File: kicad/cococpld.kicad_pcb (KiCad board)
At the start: 2 copper layers, 83.3 x 98.3 mm, 48 parts, among them IC1 ATMEGA2560-A, P1 TST, P10 COCOBUS, P11 SERIAL, P12 BARREL_JACK, P13 TST, P14 TST, P2 TST, P3 JTAG, P4 TST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

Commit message: datestamp?
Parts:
- moved P8 3.30 mm to (93.2, 142.0)
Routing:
- net /Coco interface/TCK: track 129.4 -> 135.0 mm
- net /Coco interface/SD_SS_33: track 53.8 -> 57.5 mm
- net /Coco interface/MOSI_33: track 80.7 -> 84.2 mm
- net /Coco interface/SCLK_33: track 57.4 -> 60.9 mm
- net +3.3V: track 336.5 -> 339.7 mm
- net /Microcontroller/MISO: track 90.6 -> 93.6 mm
- net GND: track 697.2 -> 696.7 mm

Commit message: start of additional goodness and fixes
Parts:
- added D10: A0, LED-1206, F.Cu at (135.1, 69.6)
- added D11: A1, LED-1206, F.Cu at (135.1, 79.8)
- added D12: A2, LED-1206, F.Cu at (135.4, 74.7)
- added D13: A3, LED-1206, F.Cu at (134.9, 65.5)
- added D8: CP, LED-1206, F.Cu at (115.1, 85.6)
- added D9: EP, LED-1206, F.Cu at (115.3, 93.5)
- added P15: JTAG SEL, pin_array_3x2, F.Cu at (68.3, 142.2)
- added P16: ICSP, pin_array_3x2, F.Cu at (39.1, 85.3)
- added R5: 150, SM0805, F.Cu at (109.5, 93.5)
- added RP2: 150, CAY16-J4, F.Cu at (128.0, 67.1)
- R3: value 1k -> 150
- R4: value R -> 47k
- moved R3 22.0 mm to (109.2, 85.6)
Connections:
- IC1 pad 15: (no net) -> /Microcontroller/LED0
- IC1 pad 16: (no net) -> /Microcontroller/LED1
- IC1 pad 17: (no net) -> /Microcontroller/LED2
- IC1 pad 18: (no net) -> /Microcontroller/LED3
- P3 pad 3: /Microcontroller/TDO -> /TDO
- P3 pad 9: /Coco interface/TDI -> /TDI
- R3 pad 1: +5V -> /Coco interface/C_POWER
- R3 pad 2: /Microcontroller/MODE -> N-0000048
- U2 pad 104: /Microcontroller/TDI -> /Coco interface/TDO
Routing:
- net GND: track 696.7 -> 0.00 mm, vias 9 -> 0
- net +3.3V: track 339.7 -> 0.00 mm, vias 5 -> 0
- net /Coco interface/C_D0: track 202.5 -> 0.00 mm, vias 1 -> 0
- net /Coco interface/~RESET: track 163.3 -> 0.00 mm, vias 2 -> 0
- net +5V: track 140.2 -> 0.00 mm, vias 2 -> 0
- net /Coco interface/TCK: track 135.0 -> 0.00 mm
- net /Coco interface/TMS: track 119.0 -> 0.00 mm, vias 2 -> 0
- net /Coco interface/C_QCLK: track 117.1 -> 0.00 mm
- net /Coco interface/C_POWER: track 104.2 -> 0.00 mm, vias 2 -> 0
- net /Coco interface/C_~HALT: track 98.3 -> 0.00 mm, vias 2 -> 0
- net /Microcontroller/MISO: track 93.6 -> 0.00 mm, vias 1 -> 0
- net /Coco interface/C_ECLK: track 87.5 -> 0.00 mm, vias 5 -> 0
- net /Coco interface/MOSI_33: track 84.2 -> 0.00 mm, vias 2 -> 0
- net /Coco interface/C_~CART: track 80.6 -> 0.00 mm, vias 1 -> 0
- net /Coco interface/LED1: track 78.8 -> 0.00 mm, vias 2 -> 0
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- removed copper zone on B.Cu, net GND
- removed copper zone on F.Cu, net GND
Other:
- board text added: "Coco Bus Interface v2.1"
- board text removed: "Coco Bus Interface v2.0"

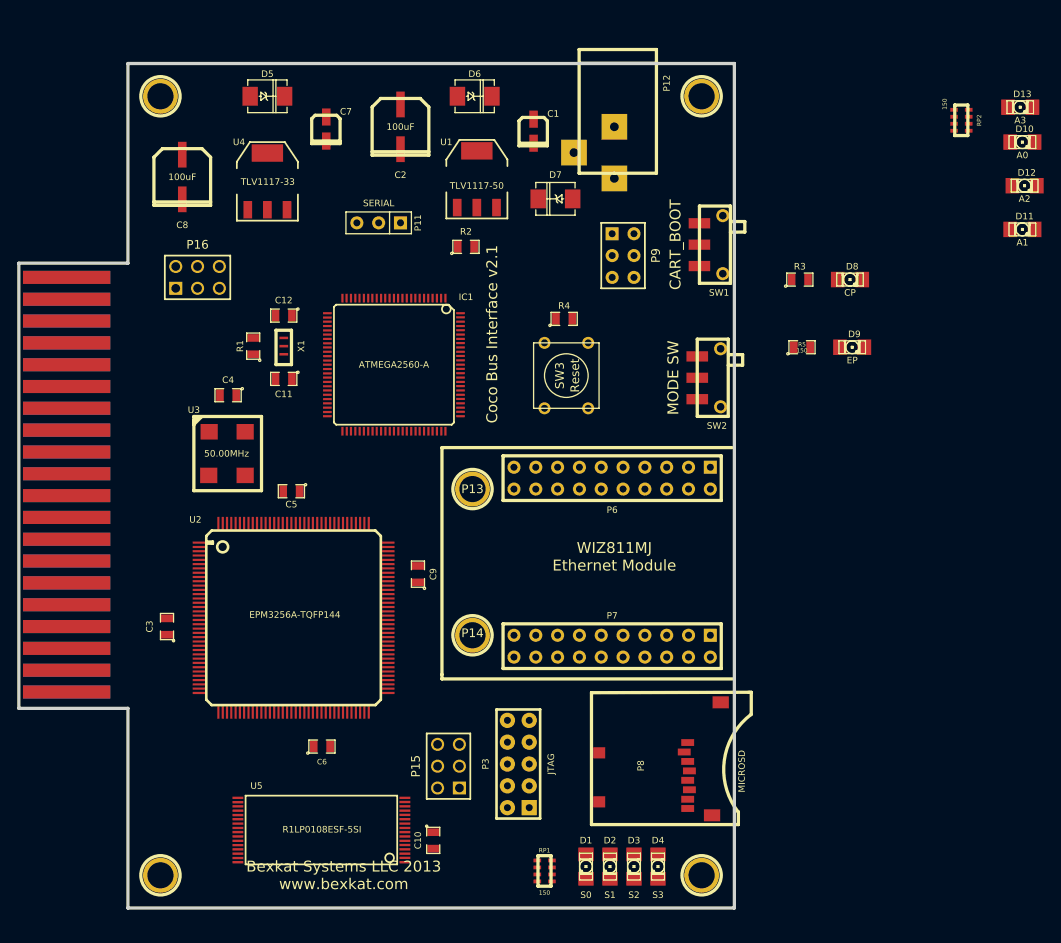
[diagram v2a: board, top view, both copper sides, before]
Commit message: initial pass for v2.1 board layout
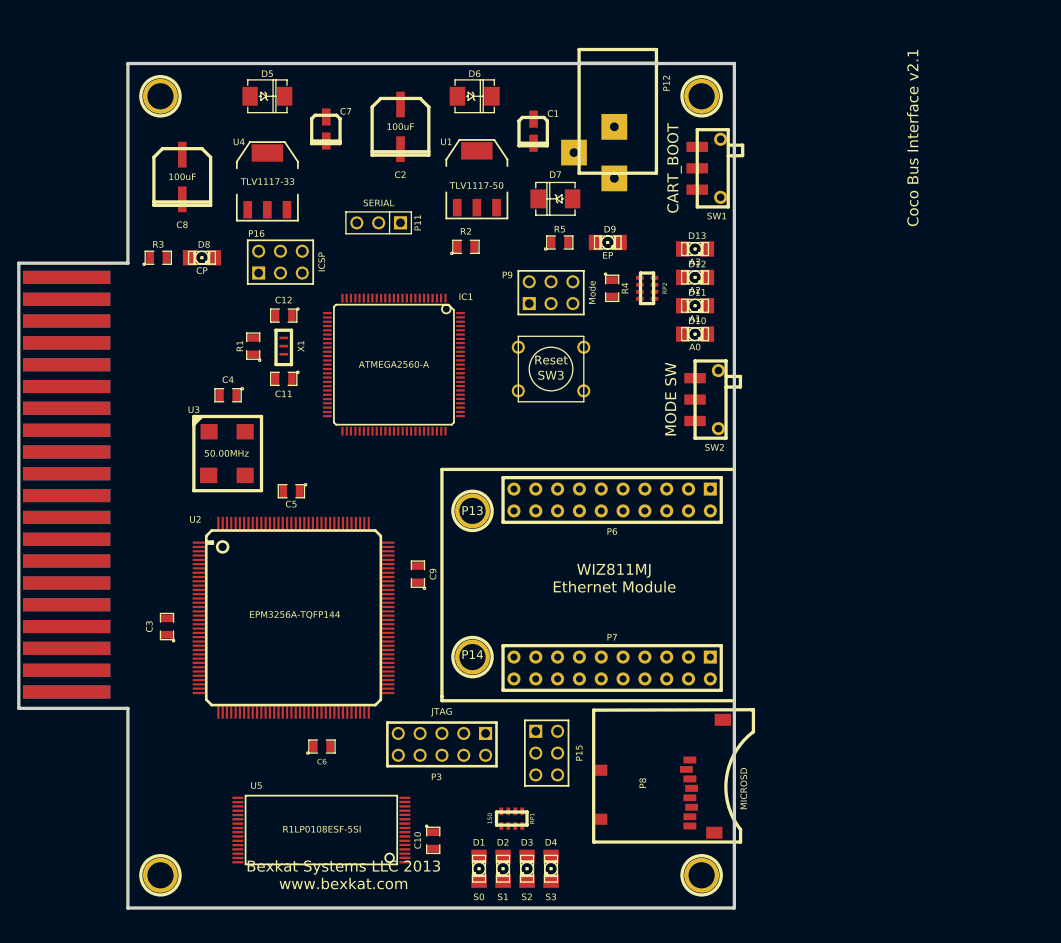
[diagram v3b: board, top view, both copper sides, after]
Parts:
- moved D8 75.5 mm to (39.6, 83.1)
- moved R3 74.7 mm to (34.5, 83.1)
- moved D10 44.2 mm to (97.0, 91.9)
- moved RP2 41.5 mm to (91.4, 86.6)
- moved D13 41.3 mm to (97.0, 82.0)
- moved D12 39.8 mm to (97.0, 85.3)
- moved D11 39.1 mm to (97.0, 88.6)
- moved D9 31.0 mm to (86.9, 81.3)
- moved R5 30.7 mm to (81.3, 81.3)
- moved D1 12.4 mm to (71.9, 154.2)
- moved D2 12.4 mm to (74.7, 154.2)
- moved D3 12.4 mm to (77.5, 154.2)
- moved D4 12.4 mm to (80.3, 154.2)
- moved P15 11.5 mm to (79.8, 140.7), turned to 270 degrees
- moved P16 9.81 mm to (48.8, 83.6)
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
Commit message: new board route
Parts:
- moved D10 2.29 mm to (97.0, 89.7)
- moved D11 1.52 mm to (97.0, 87.1)
- moved P8 1.30 mm to (92.2, 144.3)
- moved RP2 0.92 mm to (91.9, 85.9)
- moved D12 0.76 mm to (97.0, 84.6)
- moved P15 0.51 mm to (79.2, 140.7)
- moved SW1 0.25 mm to (95.8, 72.6)
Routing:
- net GND: track 0.00 -> 706.1 mm, vias 0 -> 5
- net +3.3V: track 0.00 -> 300.4 mm, vias 0 -> 7
- net /Coco interface/C_D4: track 0.00 -> 189.4 mm, vias 0 -> 1
- net /Coco interface/~RESET: track 0.00 -> 175.1 mm, vias 0 -> 3
- net +5V: track 0.00 -> 132.0 mm
- net /Coco interface/C_QCLK: track 0.00 -> 106.3 mm
- net /Microcontroller/MISO: track 0.00 -> 106.1 mm, vias 0 -> 1
- net /Coco interface/C_POWER: track 0.00 -> 105.9 mm, vias 0 -> 1
- net /Coco interface/TMS: track 0.00 -> 101.7 mm, vias 0 -> 3
- net /Coco interface/C_A13: track 0.00 -> 92.4 mm, vias 0 -> 2
- net /Coco interface/C_~CART: track 0.00 -> 89.9 mm, vias 0 -> 1
- net /Coco interface/LED2: track 0.00 -> 81.5 mm, vias 0 -> 2
- net /Coco interface/MOSI_33: track 0.00 -> 80.6 mm, vias 0 -> 2
- net /Microcontroller/SCK: track 0.00 -> 78.6 mm, vias 0 -> 2
- net /Coco interface/C_~NMI: track 0.00 -> 70.9 mm, vias 0 -> 3
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
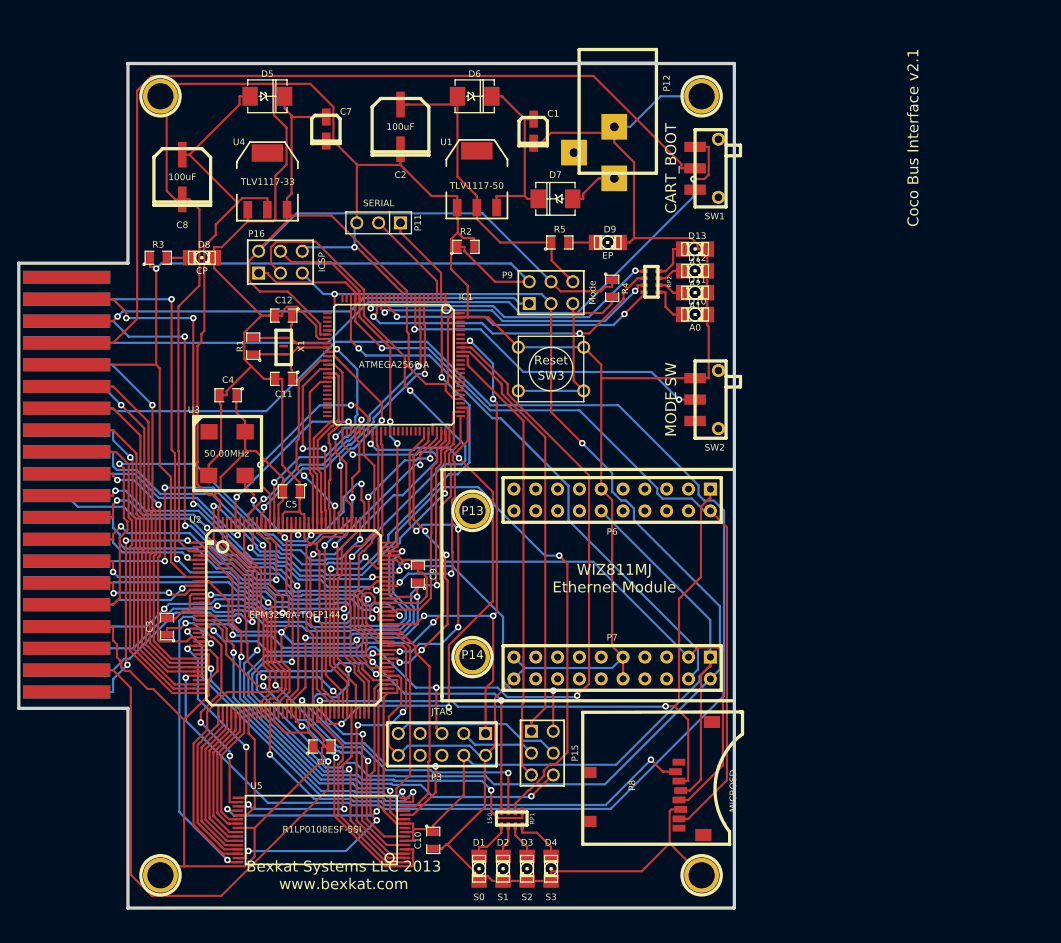
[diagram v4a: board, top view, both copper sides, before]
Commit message: first draft of v2.1 hardware.  Added some addition diagnostic leds, power indicators, and a separate SPI interface for the 5v side.  Maybe add support for external LCD?
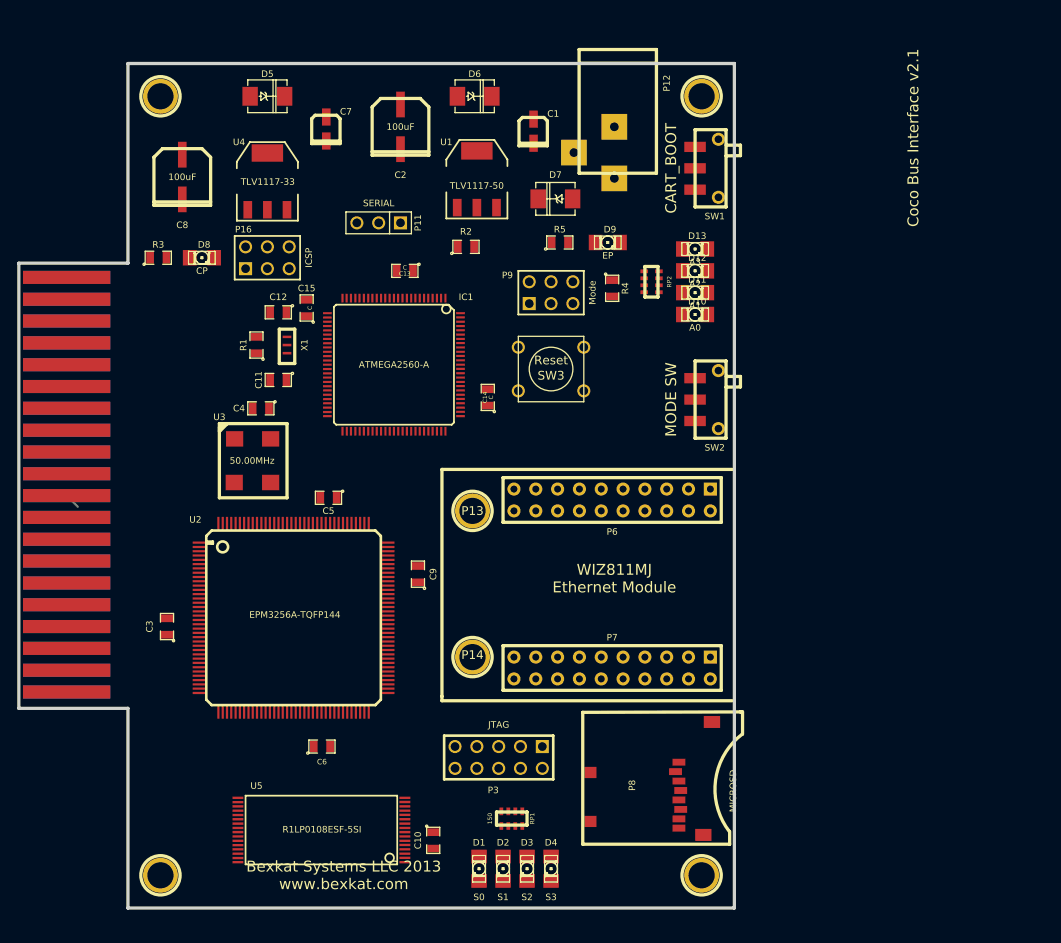
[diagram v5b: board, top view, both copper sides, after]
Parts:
- removed P15: JTAG SEL, pin_array_3x2
- added C13: C, SM0805, F.Cu at (63.2, 84.6)
- added C14: C, SM0805, F.Cu at (72.9, 99.3)
- added C15: C, SM0805, F.Cu at (51.8, 88.9)
- moved P3 6.78 mm to (74.2, 141.2)
- moved C5 4.38 mm to (54.4, 111.0)
- moved C4 4.10 mm to (46.5, 100.6)
- moved U3 3.08 mm to (45.5, 106.7)
- moved P16 1.61 mm to (47.2, 83.1)
- moved C12 0.74 mm to (48.5, 89.4)
- moved C11 0.65 mm to (48.5, 97.3)
- moved X1 0.40 mm to (49.5, 93.2)
- moved R1 0.40 mm to (46.0, 93.2)
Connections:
- P3 pad 3: /TDO -> /Microcontroller/TDO
- P3 pad 9: /TDI -> /Coco interface/TDI
- U2 pad 104: /Coco interface/TDO -> /Microcontroller/TDI
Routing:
- net GND: track 706.1 -> 0.00 mm, vias 5 -> 0
- net +3.3V: track 300.4 -> 0.00 mm, vias 7 -> 0
- net /Coco interface/C_D4: track 189.4 -> 0.00 mm, vias 1 -> 0
- net /Coco interface/~RESET: track 175.1 -> 0.00 mm, vias 3 -> 0
- net +5V: track 132.0 -> 0.00 mm
- net /Coco interface/C_QCLK: track 106.3 -> 0.00 mm
- net /Microcontroller/MISO: track 106.1 -> 0.00 mm, vias 1 -> 0
- net /Coco interface/C_POWER: track 105.9 -> 0.00 mm, vias 1 -> 0
- net /Coco interface/TMS: track 101.7 -> 0.00 mm, vias 3 -> 0
- net /Coco interface/C_A13: track 92.4 -> 0.00 mm, vias 2 -> 0
- net /Coco interface/C_~CART: track 89.9 -> 0.00 mm, vias 1 -> 0
- net /Coco interface/LED2: track 81.5 -> 0.00 mm, vias 2 -> 0
- net /Coco interface/MOSI_33: track 80.6 -> 0.00 mm, vias 2 -> 0
- net /Microcontroller/SCK: track 78.6 -> 0.00 mm, vias 2 -> 0
- net /Coco interface/C_~NMI: track 70.9 -> 0.00 mm, vias 3 -> 0
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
